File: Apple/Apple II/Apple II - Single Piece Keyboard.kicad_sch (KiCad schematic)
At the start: 0 parts

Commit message: More Apple II schematic work
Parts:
- added KBD?: SPK_SINGLE_PIECE_KEYBOARD, symbol Apple II:SPK_SINGLE_PIECE_KEYBOARD
- added U?: SPK_U5_MM5740, symbol Apple II:SPK_U5_MM5740
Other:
- title: (none) -> Apple II - Single Piece Keyboard
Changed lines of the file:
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@@
 (kicad_sch (version 20211123) (generator eeschema)
-  (paper "A4")
+  (paper "A3")
   (title_block
+    (title "Apple II - Single Piece Keyboard")
     (date "2022-07-11")
+    (rev "SPK")
     (company "Apple Computers, Inc.")
     (comment 1 "Original schematic by Apple Computers")
@@
     (comment 4 "Source: The Apple II Circuit Description by W. Gayler")
   )
+  (symbol (lib_id "Apple II:SPK_U5_MM5740") (at 207.01 33.02 0) (unit 1)
+    (in_bom yes) (on_board yes) (fields_autoplaced)
+    (property "Reference" "U?" (id 0) (at 186.69 12.7 0)
+      (effects (font (size 1.27 1.27)) hide)
+    )
+    (property "Value" "SPK_U5_MM5740" (id 1) (at 186.69 15.24 0)
+      (effects (font (size 1.27 1.27)) hide)
+    )
+    (property "Footprint" "" (id 2) (at 186.69 12.7 0)
+      (effects (font (size 1.27 1.27)) hide)
+    )
+    (property "Datasheet" "" (id 3) (at 186.69 12.7 0)
+      (effects (font (size 1.27 1.27)) hide)
+    )
+    (pin "23")
+    (pin "1")
+    (pin "10")
+    (pin "11")
+    (pin "12")
+    (pin "13")
+    (pin "14")
+    (pin "15")
+    (pin "16")
+    (pin "17")
+    (pin "18")
+    (pin "19")
+    (pin "2")
+    (pin "20")
+    (pin "21")
+    (pin "22")
+    (pin "24")
+    (pin "25")
+    (pin "26")
+    (pin "27")
+    (pin "28")
+    (pin "29")
+    (pin "3")
+    (pin "30")
+    (pin "31")
+    (pin "32")
+    (pin "33")
+    (pin "34")
+    (pin "35")
+    (pin "36")
+    (pin "37")
+    (pin "38")
+    (pin "39")
+    (pin "4")
+    (pin "40")
+    (pin "5")
+    (pin "6")
+    (pin "7")
+    (pin "8")
+    (pin "9")
+  )
+  (symbol (lib_id "Apple II:SPK_SINGLE_PIECE_KEYBOARD") (at 34.29 30.48 0) (unit 1)
+    (in_bom yes) (on_board yes) (fields_autoplaced)
+    (property "Reference" "KBD?" (id 0) (at -10.16 -5.08 0)
+      (effects (font (size 1.27 1.27)) hide)
+    )
+    (property "Value" "SPK_SINGLE_PIECE_KEYBOARD" (id 1) (at -10.16 -7.62 0)
+      (effects (font (size 1.27 1.27)) hide)
+    )
+    (property "Footprint" "" (id 2) (at -10.16 -7.62 0)
+      (effects (font (size 1.27 1.27)) hide)
+    )
+    (property "Datasheet" "" (id 3) (at -10.16 -7.62 0)
+      (effects (font (size 1.27 1.27)) hide)
+    )
+    (pin "X1")
+    (pin "X2")
+    (pin "X3")
+    (pin "X4")
+    (pin "X5")
+    (pin "X6")
+    (pin "X7")
+    (pin "X8")
+    (pin "X9")
+    (pin "Y1")
+    (pin "Y10")
+    (pin "Y2")
+    (pin "Y3")
+    (pin "Y4")
+    (pin "Y5")
+    (pin "Y6")
+    (pin "Y7")
+    (pin "Y8")
+    (pin "Y9")
+  )
 )

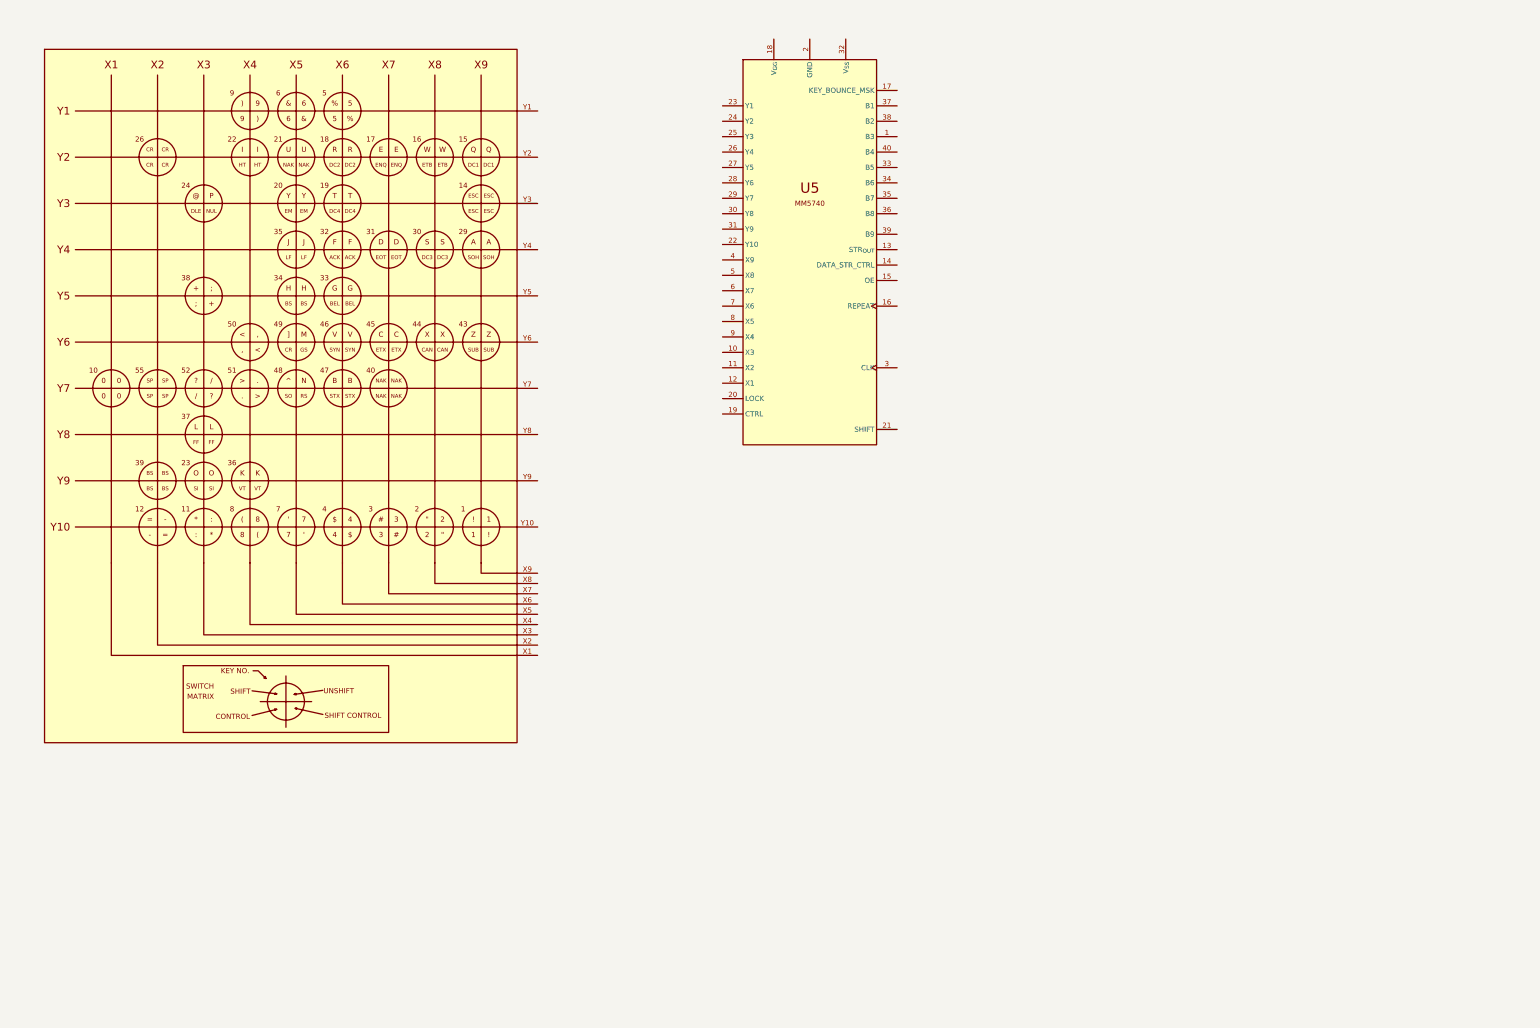
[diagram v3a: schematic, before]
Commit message: Finished Apple II - Single Piece Keyboard
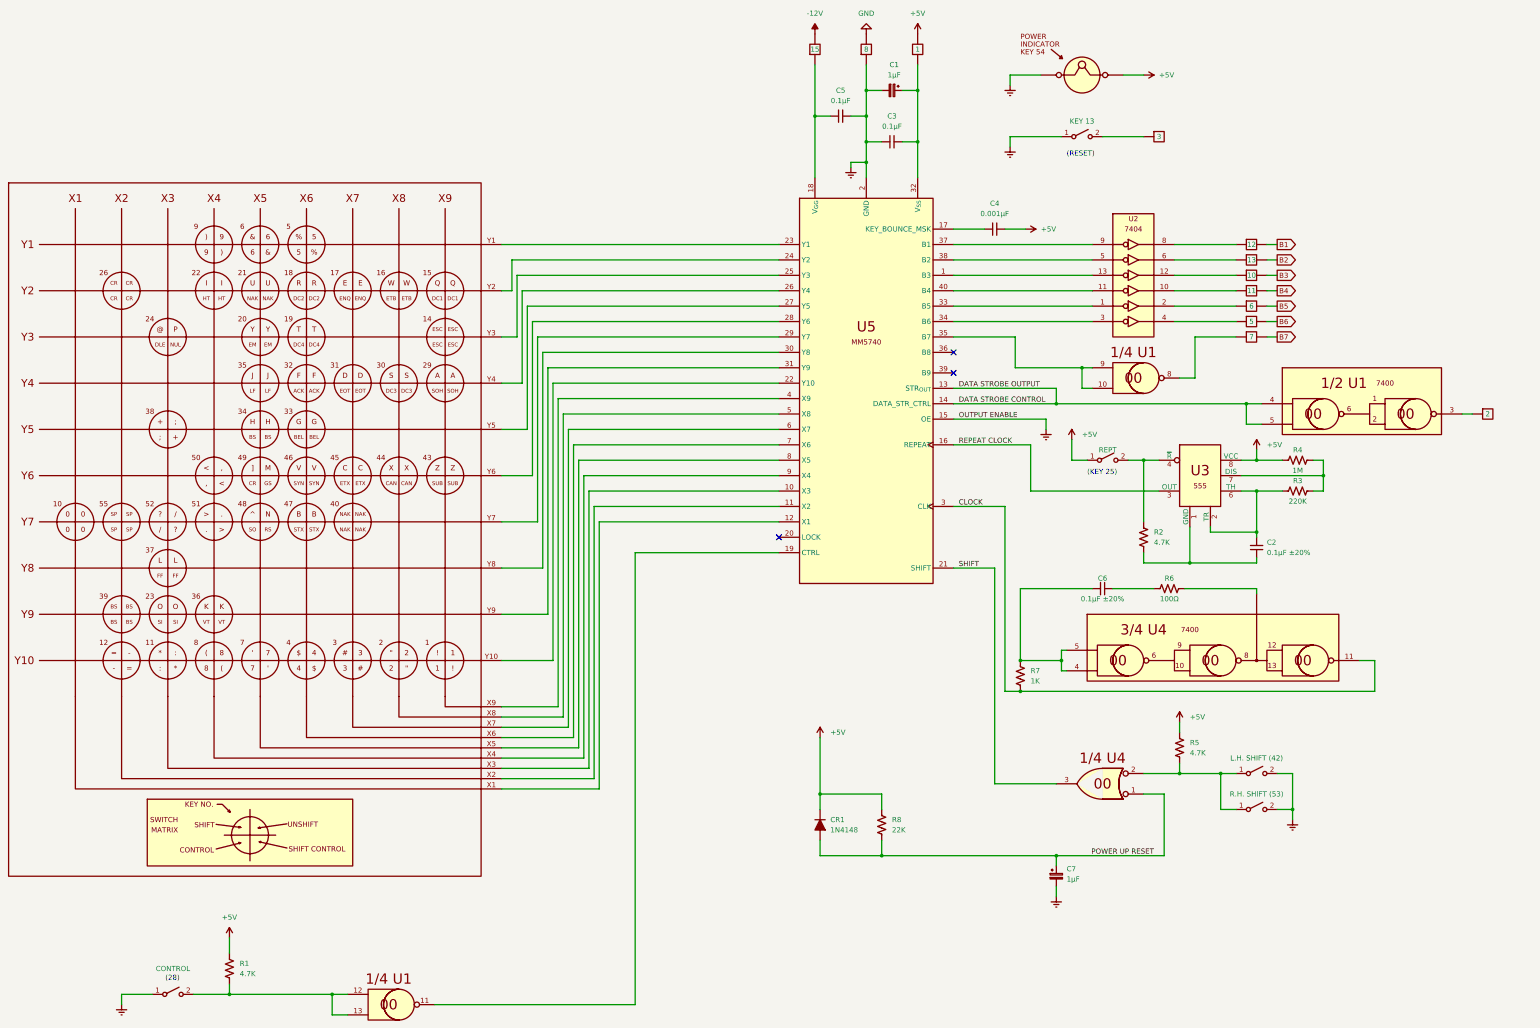
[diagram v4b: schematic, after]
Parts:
- added C1, C7: 1µF, symbol Device:C_Polarized_Small
- added C2, C6: 0.1µF ±20%, symbol Device:C_Small
- added C3, C5: 0.1µF, symbol Device:C_Small
- added C4: 0.001µF, symbol Device:C_Small
- added CR1: 1N4148, symbol Device:D_Filled
- added D?: SPK_POWER_INDICATOR_KEY54, symbol Apple II:SPK_POWER_INDICATOR_KEY54
- added KBDN1: 1, symbol Apple II:KBD_NOTE_J1_2PIN
- added KBDN10: 10, symbol Apple II:KBD_NOTE_J1_2PIN
- added KBDN11: 11, symbol Apple II:KBD_NOTE_J1_2PIN
- added KBDN12: 12, symbol Apple II:KBD_NOTE_J1_2PIN
- added KBDN13: 13, symbol Apple II:KBD_NOTE_J1_2PIN
- added KBDN15: 15, symbol Apple II:KBD_NOTE_J1_2PIN
- added KBDN2: 2, symbol Apple II:KBD_NOTE_J1_1PIN
- added KBDN3: 3, symbol Apple II:KBD_NOTE_J1_1PIN
- added KBDN5: 5, symbol Apple II:KBD_NOTE_J1_2PIN
- added KBDN6: 6, symbol Apple II:KBD_NOTE_J1_2PIN
- added KBDN7: 7, symbol Apple II:KBD_NOTE_J1_2PIN
- added KBDN8: 8, symbol Apple II:KBD_NOTE_J1_2PIN
- added R1, R2, R5: 4.7K, symbol Device:R_US
- added R3: 220K, symbol Device:R_US
- added R4: 1M, symbol Device:R_US
- added R6: 100Ω, symbol Device:R_US
- added R7: 1K, symbol Device:R_US
- added R8: 22K, symbol Device:R_US
- added SW13: KEY 13, symbol Switch:SW_SPST
- added SW25: REPT, symbol Switch:SW_SPST
- added SW28: CONTROL, symbol Switch:SW_SPST
- added SW42: L.H. SHIFT (42), symbol Switch:SW_SPST
- added SW53: R.H. SHIFT (53), symbol Switch:SW_SPST
- added U? (x3): SPK_U1_7400, symbol Apple II:SPK_U1_7400
- added U?: SPK_U3_555, Package_SO:SOIC-8_3.9x4.9mm_P1.27mm, symbol Apple II:SPK_U3_555
- added U? (x2): SPK_U4_7400, symbol Apple II:SPK_U4_7400
- added U?: SPK_U2_7404, symbol Apple II:SPK_U2_7404
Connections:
- net at U?.1 (B3): now also U?.13
- net at U?.10 (X3): now also KBD?.X3
- net at U?.11 (X2): now also KBD?.X2
- net at U?.12 (X1): now also KBD?.X1
- net DATA STROBE CONTROL: now reaches U?.13 (STR_{OUT})
- net DATA STROBE CONTROL: now also U?.14 (DATA_STR_CTRL), U?.4, U?.5
- net Earth: now reaches U?.15 (OE)
- net Earth: now also U?.2 (GND), C1.2, C3.1, C5.2, C7.2, D?., KBDN8., SW13.1 (A), SW28.1 (A), SW42.2 (B), SW53.2 (B)
- net REPEAT CLOCK: now reaches U?.16 (REPEAT)
- net REPEAT CLOCK: now also U?.3 (OUT)
- net at U?.17 (KEY_BOUNCE_MSK): now also C4.1
- net at U?.18 (V_{GG}): now also C5.1, KBDN15.
- net at U?.19 (CTRL): now also U?.11
- net SHIFT: now reaches U?.21 (SHIFT)
- net SHIFT: now also U?.3
- net at U?.22 (Y10): now also KBD?.Y10
- net at U?.23 (Y1): now also KBD?.Y1
- net at U?.24 (Y2): now also KBD?.Y2
- net at U?.25 (Y3): now also KBD?.Y3
- net at U?.26 (Y4): now also KBD?.Y4
- net at U?.27 (Y5): now also KBD?.Y5
- net at U?.28 (Y6): now also KBD?.Y6
- net at U?.29 (Y7): now also KBD?.Y7
- net CLOCK: now reaches U?.3 (CLK)
- net CLOCK: now also R7.1, U?.11
- net at U?.30 (Y8): now also KBD?.Y8
- net at U?.31 (Y9): now also KBD?.Y9
- net at U?.32 (V_{SS}): now also C1.1, C3.2, KBDN1.
- net at U?.33 (B5): now also U?.1
- net at U?.34 (B6): now also U?.3
- net at U?.35 (B7): now also U?.10, U?.9
- net at U?.37 (B1): now also U?.9
- net at U?.38 (B2): now also U?.5
- net at U?.4 (X9): now also KBD?.X9
- net at U?.40 (B4): now also U?.11
- net at U?.5 (X8): now also KBD?.X8
- net at U?.6 (X7): now also KBD?.X7
- net at U?.7 (X6): now also KBD?.X6
- net at U?.8 (X5): now also KBD?.X5
- net at U?.9 (X4): now also KBD?.X4
- new net: C6.1, R6.1
- new net: R6.2, U?.
- new net: C2.1, R2.1, U?.1 (GND)
- new net: R2.2, SW25.2 (B), U?.4 (~{R})
- new net: C2.2, R3.1, U?.2 (TR), U?.6 (TH)
- new net: R3.2, R4.2, U?.7 (DIS)
- new net: KBDN13., U?.6
- new net: KBDN7., U?.8
- new net: KBDN6., U?.2
- new net: KBDN2., U?.3
- new net: KBDN3., SW13.2 (B)
- new net: KBDN12., U?.8
- new net: R1.2, SW28.2 (B), U?.12, U?.13
- new net: R5.1, SW42.1 (A), SW53.1 (A), U?.2
- new net: C6.2, R7.2, U?.4, U?.5
- new net: KBDN11., U?.10
- new net: KBDN5., U?.4
- new net: KBDN10., U?.12
- new net +5V: C4.2, CR1.1 (K), D?., KBDN1., R1.1, R4.1, R5.2, R8.2, SW25.1 (A), U?.8 (VCC)
- new net -12V: KBDN15.
- new net B1: KBDN12.
- new net B2: KBDN13.
- new net B3: KBDN10.
- new net B4: KBDN11.
- new net B5: KBDN6.
- new net B6: KBDN5.
- new net B7: KBDN7.
- new net GND: KBDN8.
- new net POWER UP RESET: C7.1, CR1.2 (A), R8.1, U?.1
- no-connect marks 0 -> 3
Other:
- note added: "(28)"
- note added: "(KEY 25)"
- note added: "(RESET)"

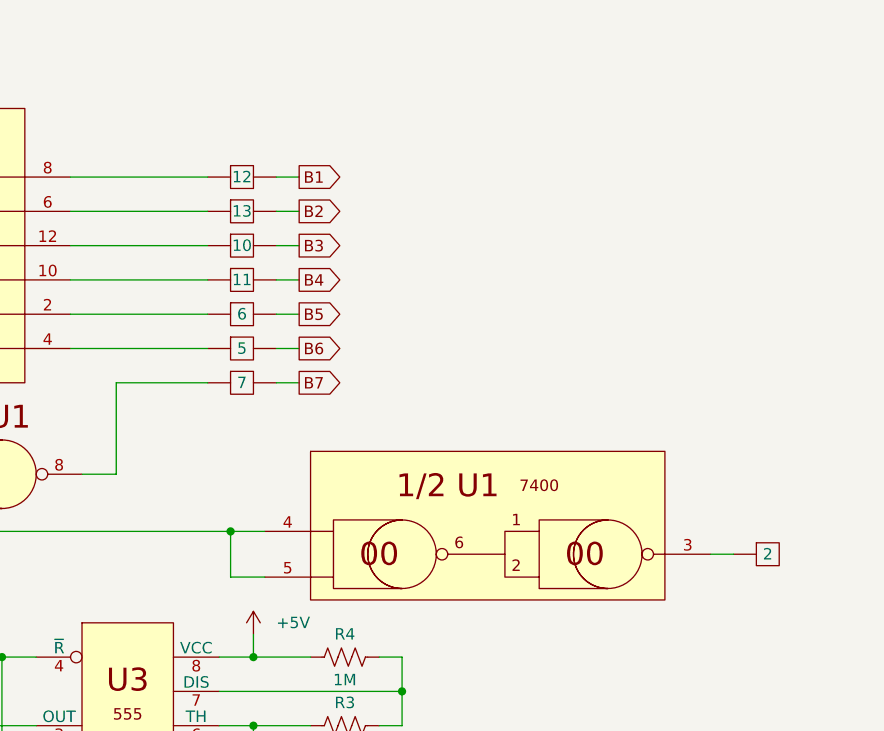
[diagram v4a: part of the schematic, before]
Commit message: Finished Apple II - Sheet 22 - Two-Piece Keyboard
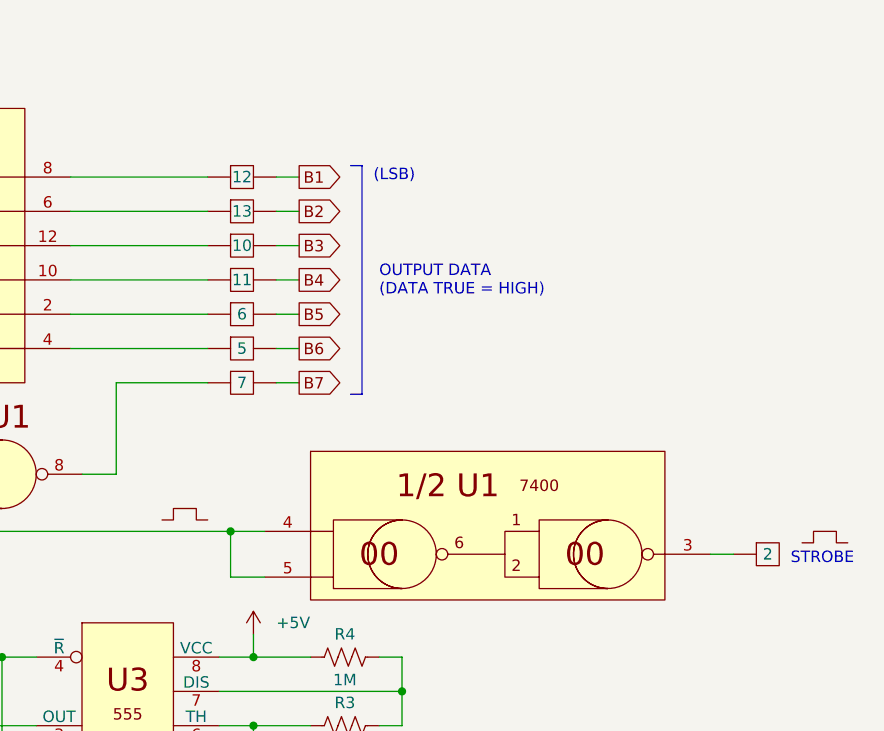
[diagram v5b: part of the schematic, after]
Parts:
- added N? (x2): SINE_WAVE, symbol Apple II:SINE_WAVE
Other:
- note added: "(LSB)"
- note added: "OUTPUT DATA (DATA TRUE = HIGH)"
- note added: "STROBE"
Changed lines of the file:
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@@
     (stroke (width 0) (type default) (color 0 0 0 0))
+  )
+  (polyline (pts (xy 346.075 77.47) (xy 346.075 102.87))
+    (stroke (width 0) (type solid) (color 0 0 0 0))
   )
   (wire (pts (xy 339.09 97.79) (xy 336.55 97.79))
@@
     (stroke (width 0) (type default) (color 0 0 0 0))
   )
+  (polyline (pts (xy 344.805 102.87) (xy 346.075 102.87))
+    (stroke (width 0) (type solid) (color 0 0 0 0))
+  )
   (wire (pts (xy 284.48 240.03) (xy 284.48 237.49))
     (stroke (width 0) (type default) (color 0 0 0 0))
@@
     (stroke (width 0) (type default) (color 0 0 0 0))
   )
+  (polyline (pts (xy 344.805 77.47) (xy 346.075 77.47))
+    (stroke (width 0) (type solid) (color 0 0 0 0))
+  )
   (wire (pts (xy 161.29 193.04) (xy 147.32 193.04))
     (stroke (width 0) (type default) (color 0 0 0 0))
@@
     (effects (font (size 1.27 1.27)) (justify left bottom))
   )
+  (text "STROBE" (at 393.7 121.92 0)
+    (effects (font (size 1.27 1.27)) (justify left bottom))
+  )
   (text "(28)" (at 64.135 260.985 0)
     (effects (font (size 1.27 1.27)) (justify left bottom))
   )
+  (text "OUTPUT DATA\n(DATA TRUE = HIGH)" (at 347.98 92.075 0)
+    (effects (font (size 1.27 1.27)) (justify left bottom))
+  )
   (text "(RESET)" (at 287.02 57.15 0)
+    (effects (font (size 1.27 1.27)) (justify left bottom))
+  )
+  (text "(LSB)" (at 347.345 79.375 0)
     (effects (font (size 1.27 1.27)) (justify left bottom))
   )
@@
     (pin "2")
   )
+  (symbol (lib_id "Apple II:SINE_WAVE") (at 397.51 119.38 0) (unit 1)
+    (in_bom yes) (on_board yes) (fields_autoplaced)
+    (property "Reference" "N?" (id 0) (at 370.84 100.33 0)
+      (effects (font (size 1.27 1.27)) hide)
+    )
+    (property "Value" "SINE_WAVE" (id 1) (at 397.51 115.57 0)
+      (effects (font (size 1.27 1.27)) hide)
+    )
+    (property "Footprint" "" (id 2) (at 397.51 118.11 0)
+      (effects (font (size 1.27 1.27)) hide)
+    )
+    (property "Datasheet" "" (id 3) (at 397.51 118.11 0)
+      (effects (font (size 1.27 1.27)) hide)
+    )
+  )
   (symbol (lib_id "Device:R_US") (at 306.07 151.13 180) (unit 1)
     (in_bom yes) (on_board yes) (fields_autoplaced)
@@
     (pin "1")
   )
+  (symbol (lib_id "Apple II:SINE_WAVE") (at 326.39 116.84 0) (unit 1)
+    (in_bom yes) (on_board yes) (fields_autoplaced)
+    (property "Reference" "N?" (id 0) (at 299.72 97.79 0)
+      (effects (font (size 1.27 1.27)) hide)
+    )
+    (property "Value" "SINE_WAVE" (id 1) (at 326.39 113.03 0)
+      (effects (font (size 1.27 1.27)) hide)
+    )
+    (property "Footprint" "" (id 2) (at 326.39 115.57 0)
+      (effects (font (size 1.27 1.27)) hide)
+    )
+    (property "Datasheet" "" (id 3) (at 326.39 115.57 0)
+      (effects (font (size 1.27 1.27)) hide)
+    )
+  )
   (symbol (lib_id "Device:C_Small") (at 231.14 46.99 90) (unit 1)
